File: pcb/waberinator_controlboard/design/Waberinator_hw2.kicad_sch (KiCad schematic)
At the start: 88 parts, among them J1 Conn_01x04_Pin, J17 GX16-4, J18 GX12-4, J19 GX12-4, J2 preconf. cable, J20 GX12-4, J21 GX12-4, J22 GX12-4, J23 GX12-4, J24 GX12-4, J25 GX12-4, J26 GX12-4, J3 preconf. cable, J4 Conn_01x08_Pin, Q1 AOSP21321, SW2 sw_te_1-1825027-1, U1 STM32F030R8Tx, U2 AMS1117-3.3, U3 LM73606QRNPRQ1, U4 LM75B

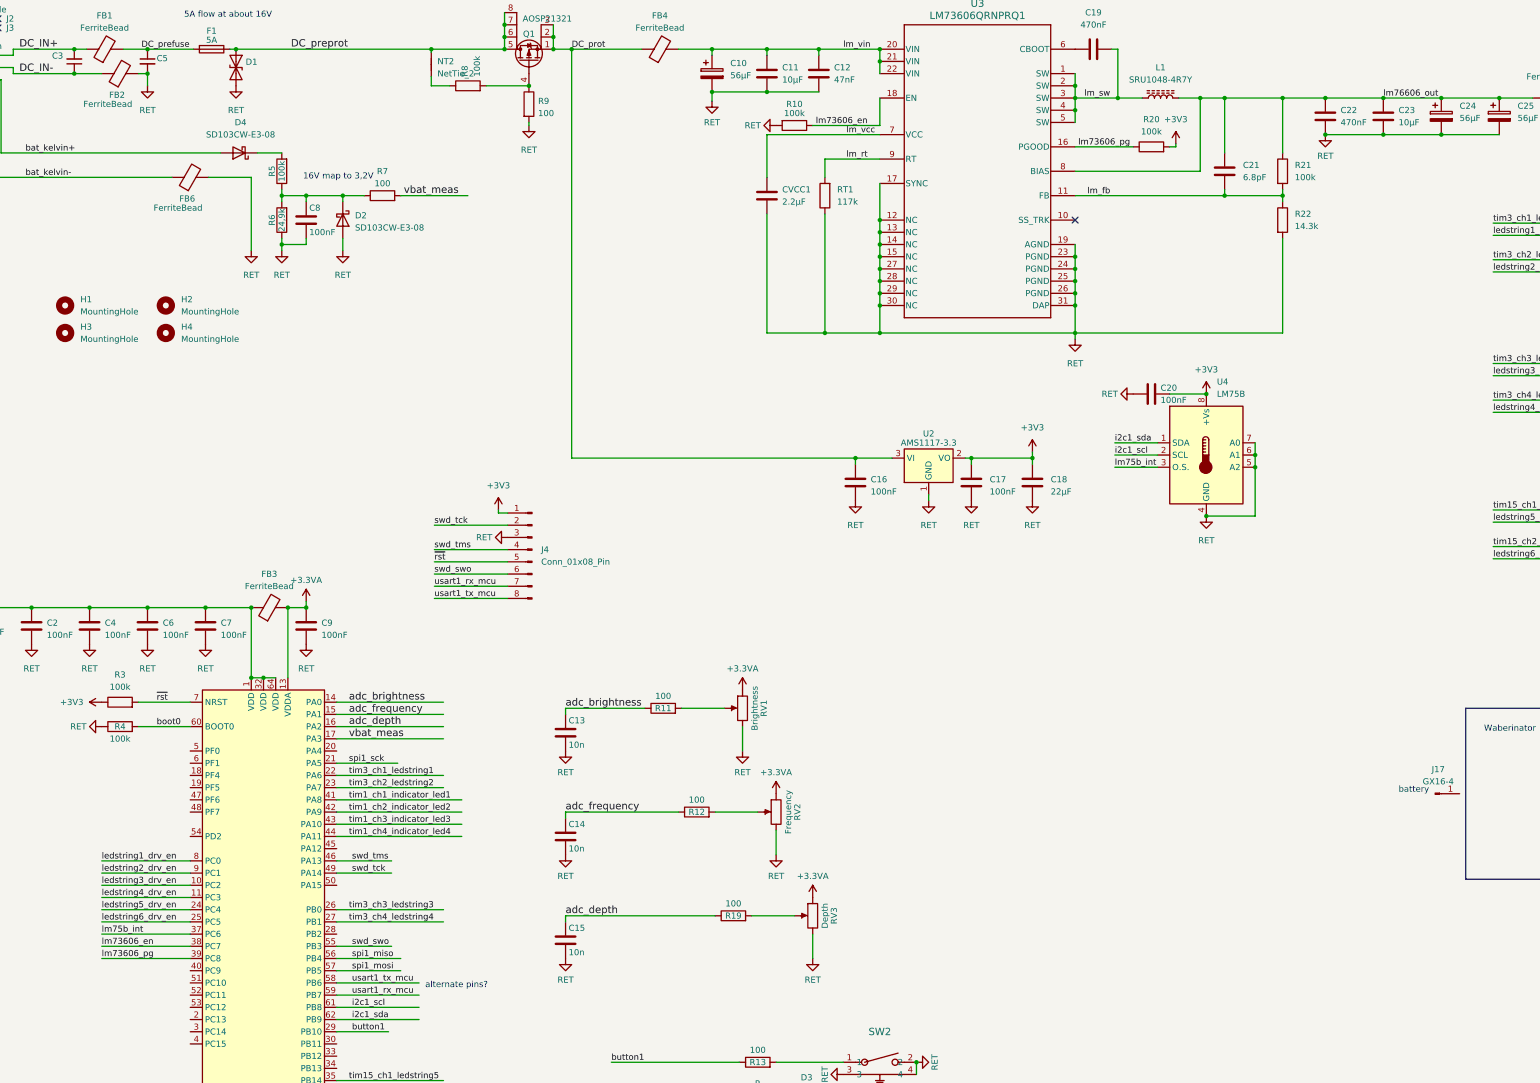
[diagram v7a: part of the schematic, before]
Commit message: [HW/FW] reshape board to get special offer, reassign some pins
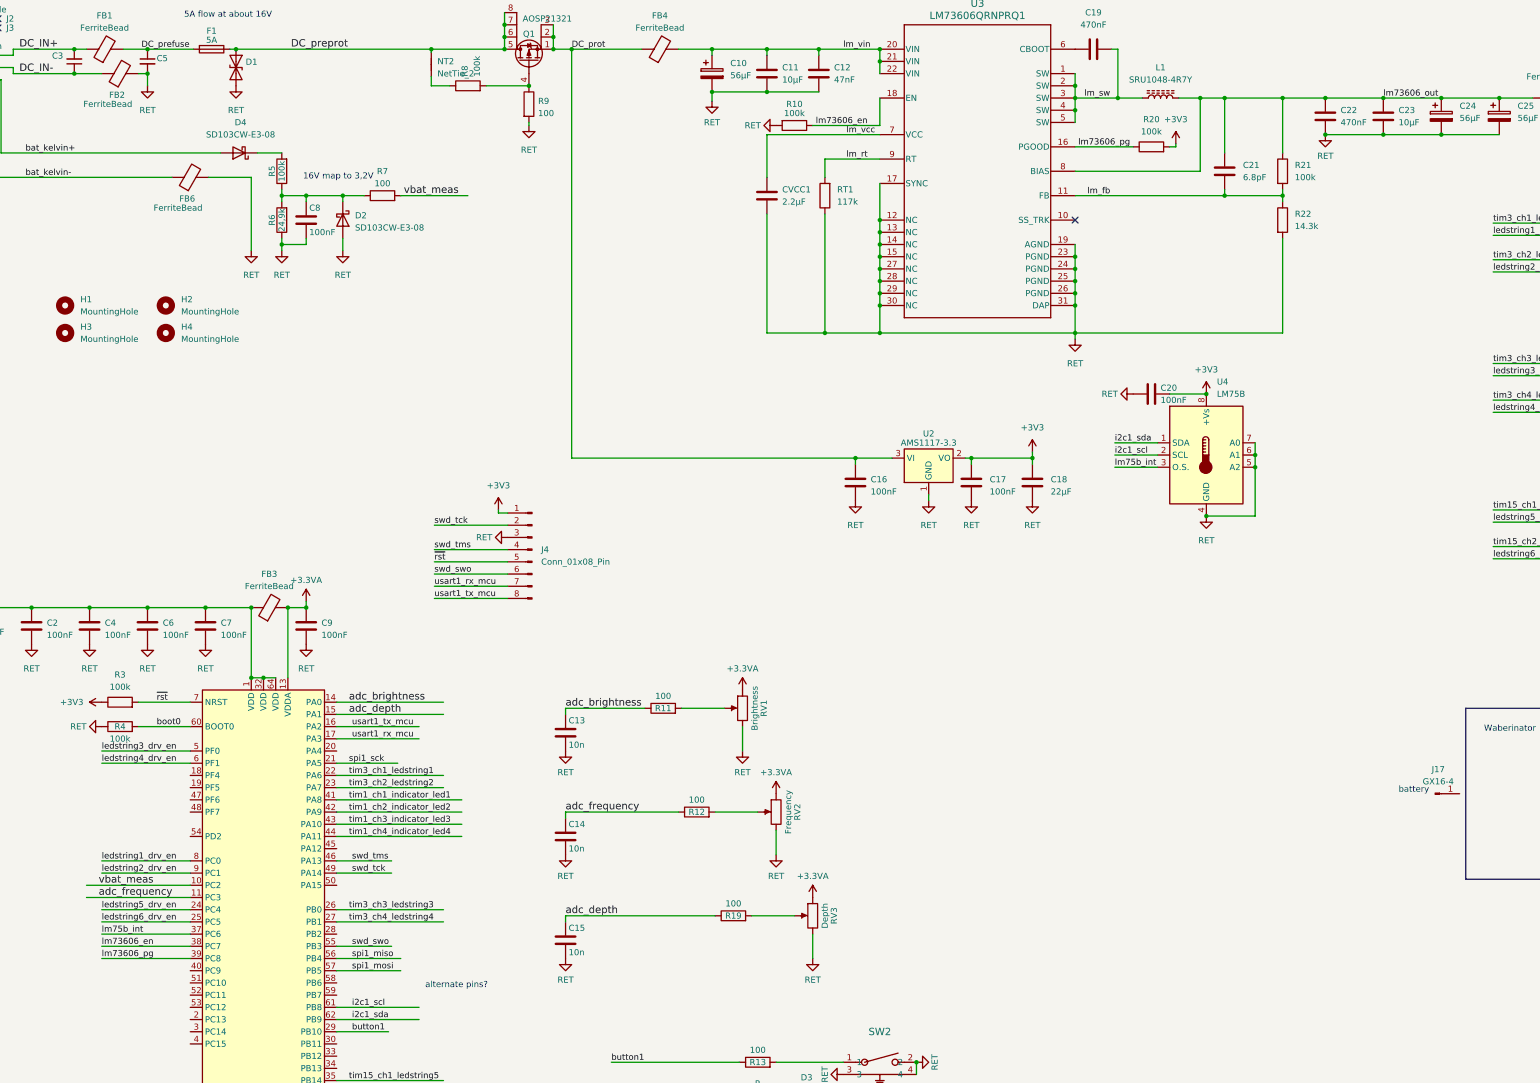
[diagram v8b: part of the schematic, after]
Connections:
- net adc_depth: now also U1.15 (PA1); no longer U1.16 (PA2)
- net adc_frequency: now also U1.11 (PC3); no longer U1.15 (PA1)
- net ledstring3_drv_en: now also U1.5 (PF0); no longer U1.10 (PC2)
- net ledstring4_drv_en: now also U1.6 (PF1); no longer U1.11 (PC3)
- net usart1_rx_mcu: now also U1.17 (PA3); no longer U1.59 (PB7)
- net usart1_tx_mcu: now also U1.16 (PA2); no longer U1.58 (PB6)
- net vbat_meas: now also U1.10 (PC2); no longer U1.17 (PA3)
- net lm76606_out renamed lm73606_out
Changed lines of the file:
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@@
     (stroke (width 0) (type default))
   )
-  (wire (pts (xy 95.25 165.1) (xy 117.475 165.1))
+  (wire (pts (xy 43.18 198.12) (xy 64.77 198.12))
     (stroke (width 0) (type default))
   )
@@
     (stroke (width 0) (type default))
   )
-  (wire (pts (xy 46.355 198.12) (xy 64.77 198.12))
+  (wire (pts (xy 46.355 170.18) (xy 64.77 170.18))
     (stroke (width 0) (type default))
   )
@@
     (stroke (width 0) (type default))
   )
-  (wire (pts (xy 95.25 167.64) (xy 117.475 167.64))
+  (wire (pts (xy 43.18 200.66) (xy 64.77 200.66))
     (stroke (width 0) (type default))
   )
@@
     (stroke (width 0) (type default))
   )
-  (wire (pts (xy 46.355 200.66) (xy 64.77 200.66))
+  (wire (pts (xy 46.355 172.72) (xy 64.77 172.72))
     (stroke (width 0) (type default))
   )
@@
     (stroke (width 0) (type default))
   )
-  (wire (pts (xy 95.25 220.98) (xy 112.395 220.98))
+  (wire (pts (xy 95.25 167.64) (xy 112.395 167.64))
     (stroke (width 0) (type default))
   )
@@
     (stroke (width 0) (type default))
   )
-  (wire (pts (xy 95.25 218.44) (xy 112.395 218.44))
+  (wire (pts (xy 95.25 165.1) (xy 112.395 165.1))
     (stroke (width 0) (type default))
   )
@@
     (effects (font (size 1.27 1.27)) (justify left bottom))
   )
-  (label "usart1_rx_mcu" (at 98.425 220.98 0) (fields_autoplaced)
+  (label "usart1_rx_mcu" (at 98.425 167.64 0) (fields_autoplaced)
     (effects (font (size 1.27 1.27)) (justify left bottom))
   )
@@
     (effects (font (size 1.27 1.27)) (justify left bottom))
   )
-  (label "usart1_tx_mcu" (at 98.425 218.44 0) (fields_autoplaced)
+  (label "usart1_tx_mcu" (at 98.425 165.1 0) (fields_autoplaced)
     (effects (font (size 1.27 1.27)) (justify left bottom))
   )
@@
     (effects (font (size 1.27 1.27)) (justify left bottom))
   )
-  (label "lm76606_out" (at 313.055 34.29 0) (fields_autoplaced)
+  (label "lm73606_out" (at 313.055 34.29 0) (fields_autoplaced)
     (effects (font (size 1.27 1.27)) (justify left bottom))
   )
@@
     (effects (font (size 1.27 1.27)) (justify left bottom))
   )
-  (label "adc_depth" (at 97.79 165.1 0) (fields_autoplaced)
+  (label "adc_depth" (at 97.79 162.56 0) (fields_autoplaced)
     (effects (font (size 1.524 1.524)) (justify left bottom))
   )
@@
     (effects (font (size 1.27 1.27)) (justify left bottom))
   )
-  (label "ledstring3_drv_en" (at 46.355 198.12 0) (fields_autoplaced)
+  (label "ledstring3_drv_en" (at 46.355 170.18 0) (fields_autoplaced)
     (effects (font (size 1.27 1.27)) (justify left bottom))
   )
@@
     (effects (font (size 1.27 1.27)) (justify left bottom))
   )
-  (label "adc_frequency" (at 97.79 162.56 0) (fields_autoplaced)
+  (label "adc_frequency" (at 45.72 200.66 0) (fields_autoplaced)
     (effects (font (size 1.524 1.524)) (justify left bottom))
   )
@@
     (effects (font (size 1.524 1.524)) (justify left bottom))
   )
-  (label "ledstring4_drv_en" (at 46.355 200.66 0) (fields_autoplaced)
+  (label "ledstring4_drv_en" (at 46.355 172.72 0) (fields_autoplaced)
     (effects (font (size 1.27 1.27)) (justify left bottom))
   )
@@
     (effects (font (size 1.27 1.27)) (justify left bottom))
   )
-  (label "vbat_meas" (at 97.79 167.64 0) (fields_autoplaced)
+  (label "vbat_meas" (at 45.72 198.12 0) (fields_autoplaced)
     (effects (font (size 1.524 1.524)) (justify left bottom))
   )
